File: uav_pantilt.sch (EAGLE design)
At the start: 7 parts

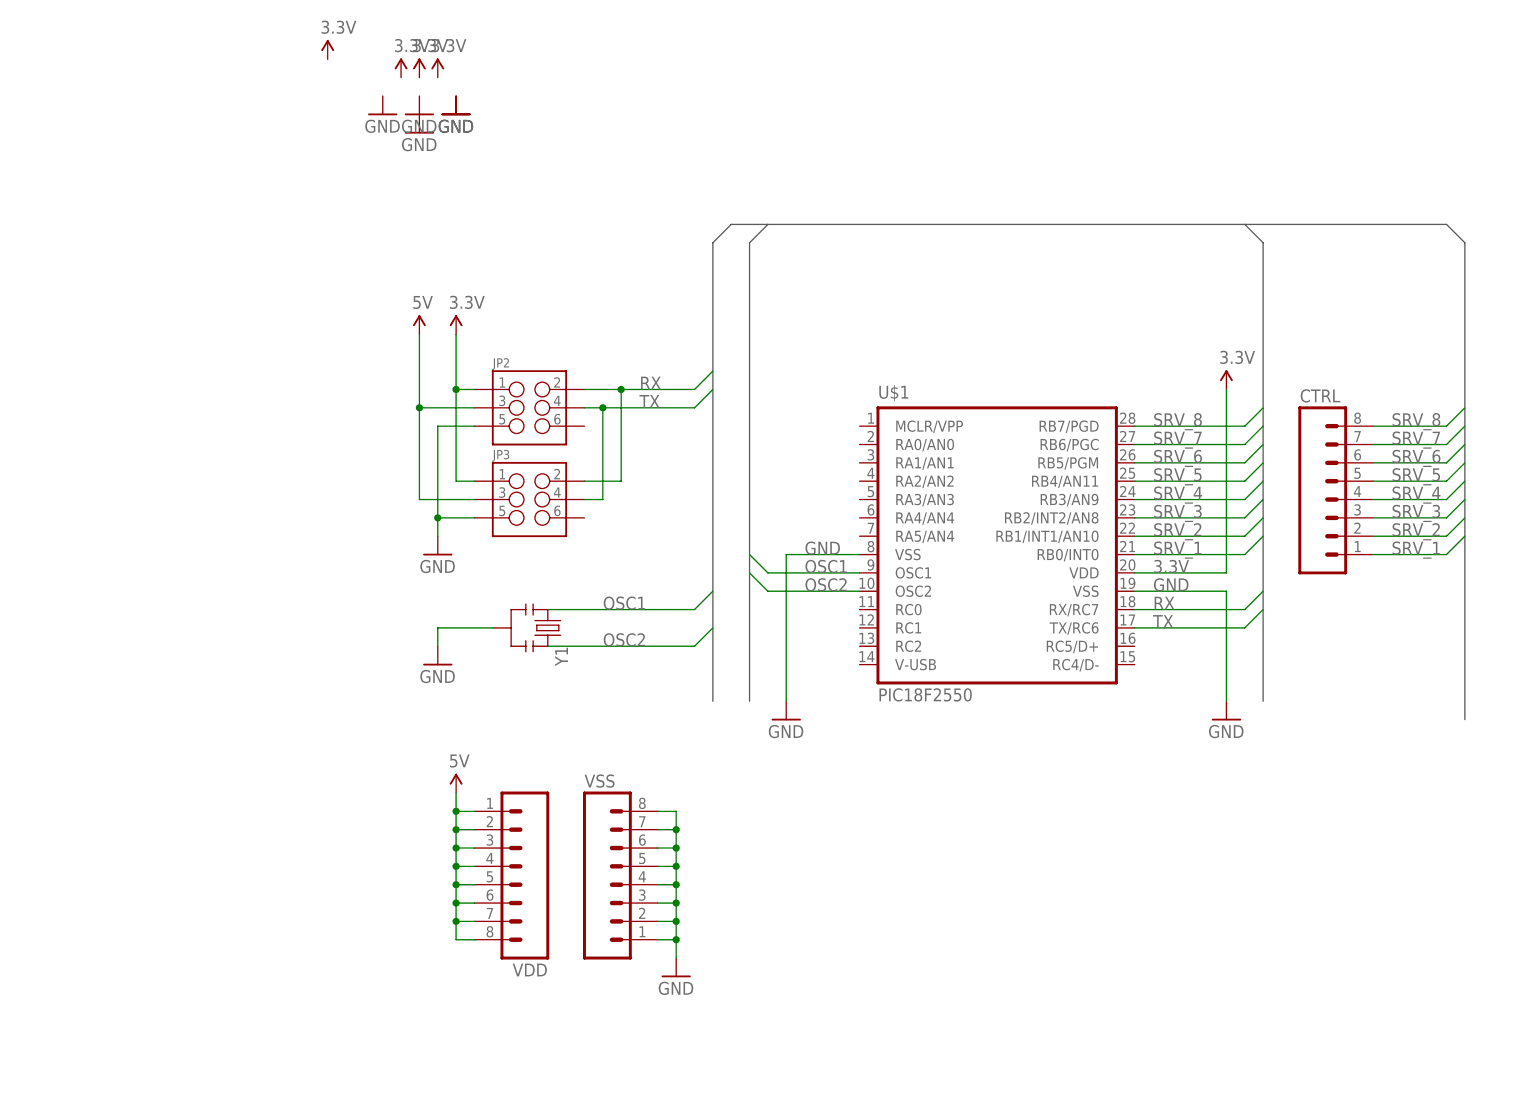
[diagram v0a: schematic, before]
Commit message: Added reset resistor, added power and BUSY led.
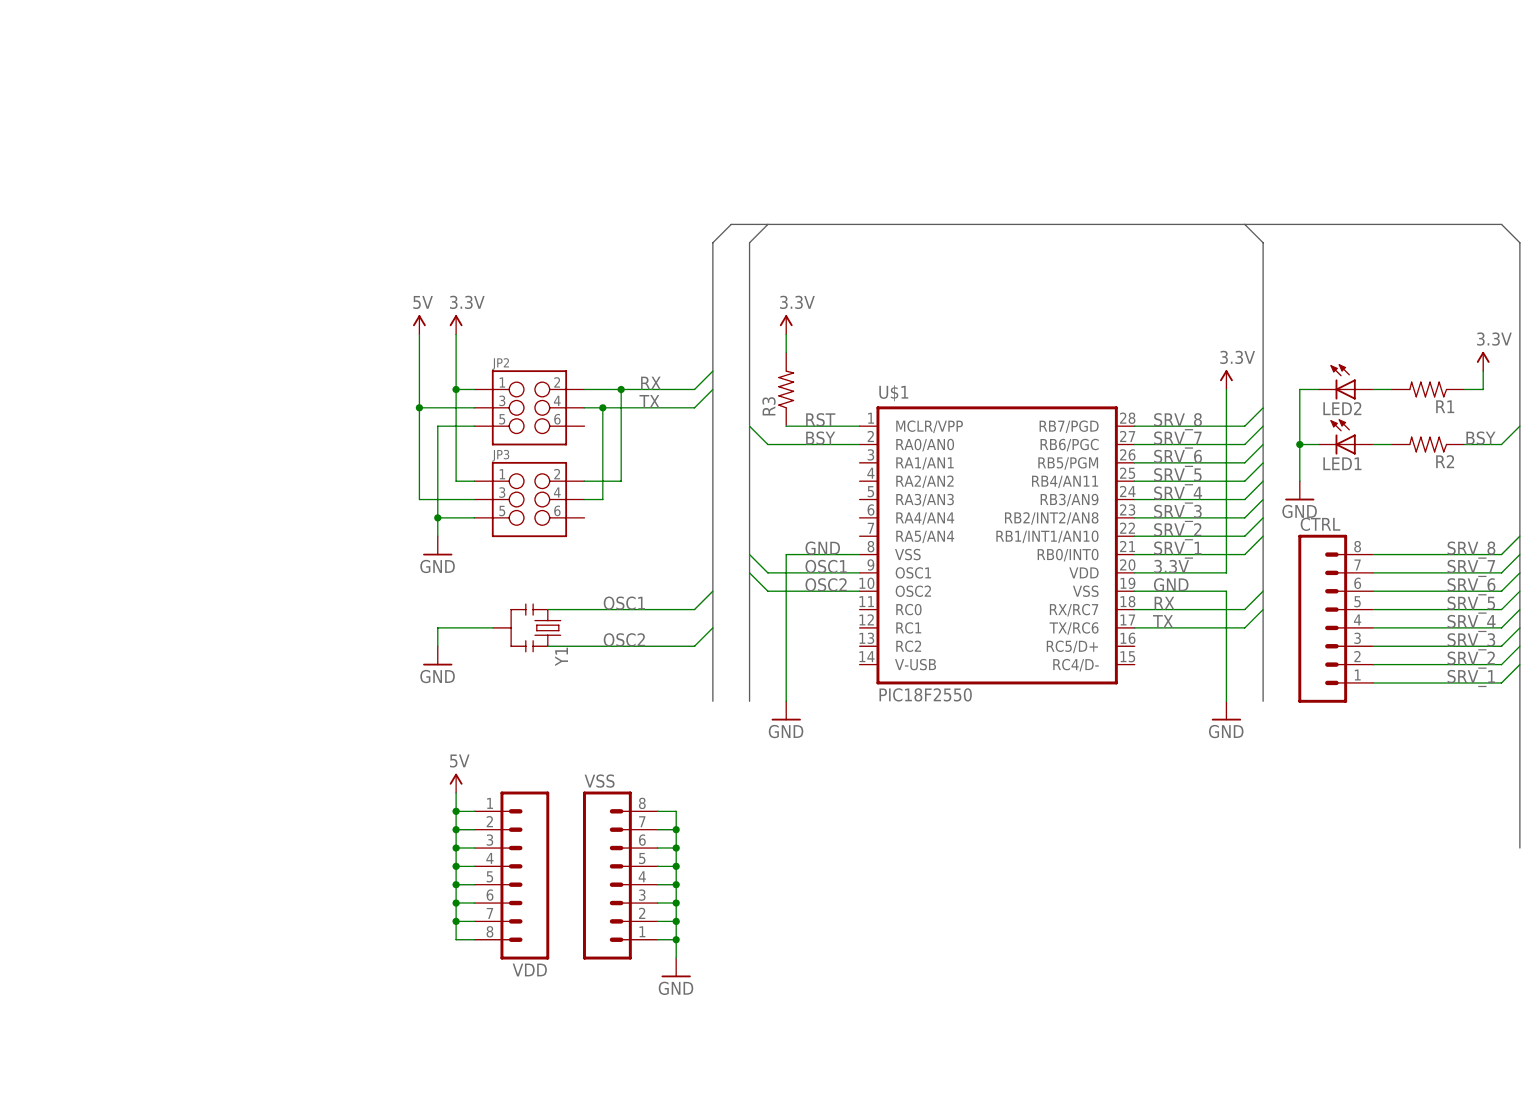
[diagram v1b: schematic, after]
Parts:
- added LED1, LED2: (no value), SparkFun-LED:LED5MM
- added R1, R2, R3: (no value), SparkFun-Resistors:RESISTORKIT
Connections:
- new net BSY: R2.1, U$1.RA0/AN0
- new net N$1: LED2.A, R1.2
- new net N$2: LED1.A, R2.2
- new net RST: R3.1, U$1.MCLR/VPP
- net 3.3V: now also R1.1, R3.2
- net GND: now also LED1.C, LED2.C
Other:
- moved on the sheet: CTRL

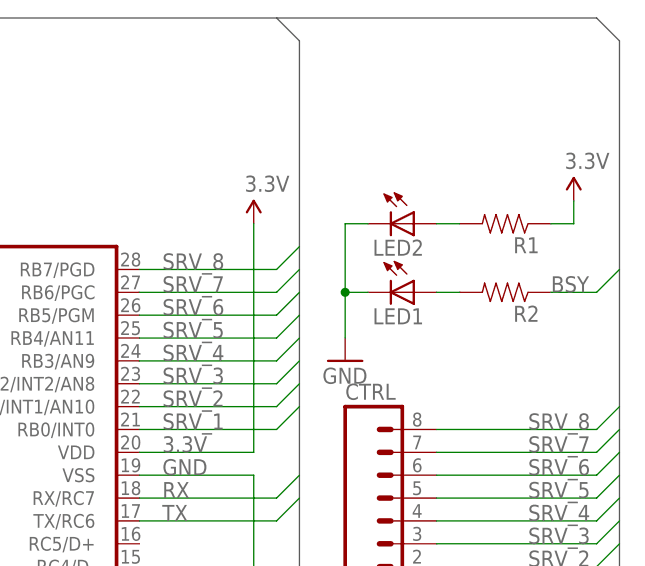
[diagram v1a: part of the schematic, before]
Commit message: Added reset resistor, added power and BUSY led.
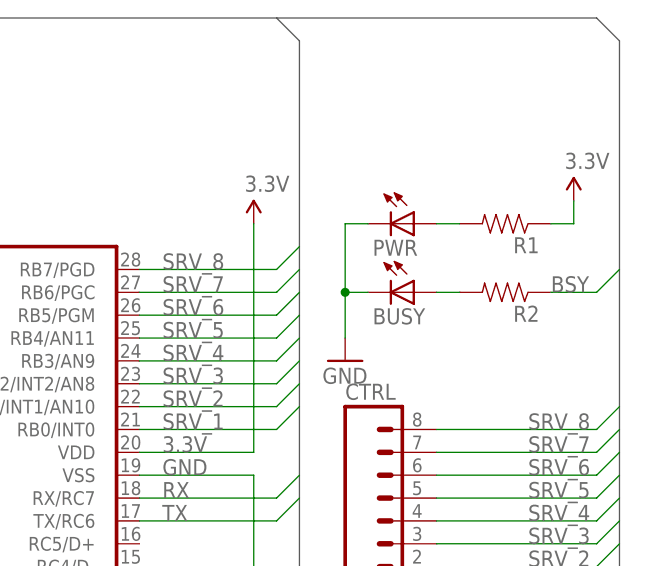
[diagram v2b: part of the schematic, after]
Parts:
- renumbered LED1 to BUSY, LED2 to PWR
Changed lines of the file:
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@@
 <part name="R1" library="SparkFun-Resistors" deviceset="RESISTOR" device="KIT"/>
 <part name="R2" library="SparkFun-Resistors" deviceset="RESISTOR" device="KIT"/>
-<part name="LED1" library="SparkFun-LED" deviceset="LED" device="5MM"/>
-<part name="LED2" library="SparkFun-LED" deviceset="LED" device="5MM"/>
+<part name="BUSY" library="SparkFun-LED" deviceset="LED" device="5MM"/>
+<part name="PWR" library="SparkFun-LED" deviceset="LED" device="5MM"/>
 <part name="R3" library="SparkFun-Resistors" deviceset="RESISTOR" device="KIT"/>
 </parts>
@@
 <instance part="R1" gate="G$1" x="170.18" y="58.42" rot="R180"/>
 <instance part="R2" gate="G$1" x="170.18" y="50.8" rot="R180"/>
-<instance part="LED1" gate="G$1" x="160.02" y="50.8" rot="R270"/>
-<instance part="LED2" gate="G$1" x="160.02" y="58.42" rot="R270"/>
+<instance part="BUSY" gate="G$1" x="160.02" y="50.8" rot="R270"/>
+<instance part="PWR" gate="G$1" x="160.02" y="58.42" rot="R270"/>
 <instance part="R3" gate="G$1" x="81.28" y="58.42" rot="R90"/>
 </instances>
@@
 </segment>
 <segment>
-<pinref part="LED2" gate="G$1" pin="C"/>
+<pinref part="PWR" gate="G$1" pin="C"/>
 <wire x1="154.94" y1="58.42" x2="152.4" y2="58.42" width="0.1524" layer="91"/>
 <wire x1="152.4" y1="58.42" x2="152.4" y2="50.8" width="0.1524" layer="91"/>
-<pinref part="LED1" gate="G$1" pin="C"/>
+<pinref part="BUSY" gate="G$1" pin="C"/>
 <wire x1="154.94" y1="50.8" x2="152.4" y2="50.8" width="0.1524" layer="91"/>
 <wire x1="152.4" y1="50.8" x2="152.4" y2="45.72" width="0.1524" layer="91"/>
@@
 <net name="N$1" class="0">
 <segment>
-<pinref part="LED2" gate="G$1" pin="A"/>
+<pinref part="PWR" gate="G$1" pin="A"/>
 <pinref part="R1" gate="G$1" pin="2"/>
 <wire x1="165.1" y1="58.42" x2="162.56" y2="58.42" width="0.1524" layer="91"/>
@@
 <net name="N$2" class="0">
 <segment>
-<pinref part="LED1" gate="G$1" pin="A"/>
+<pinref part="BUSY" gate="G$1" pin="A"/>
 <pinref part="R2" gate="G$1" pin="2"/>
 <wire x1="165.1" y1="50.8" x2="162.56" y2="50.8" width="0.1524" layer="91"/>
